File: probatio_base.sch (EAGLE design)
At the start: 12 parts

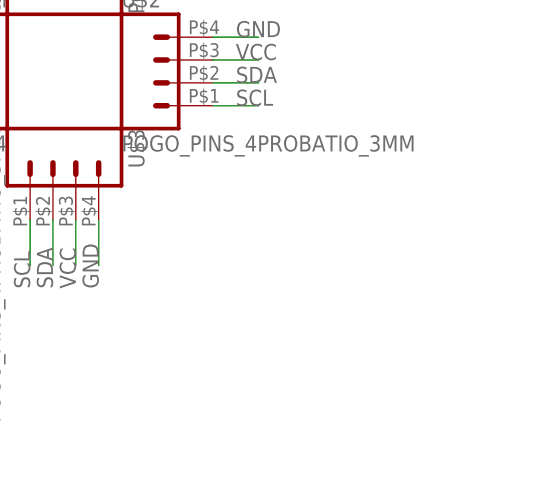
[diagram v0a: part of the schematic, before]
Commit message: added batebit logo
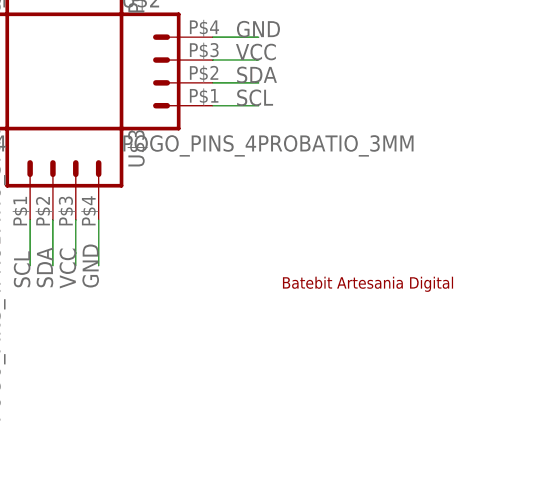
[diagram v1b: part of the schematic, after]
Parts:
- added U$13: BATEBIT_PEQ, Batebit:BATEBIT_PEQ
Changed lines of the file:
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@@
 <part name="U$11" library="Batebit" deviceset="M04" device="WIRE_PAD"/>
 <part name="U$12" library="Batebit" deviceset="M04" device="WIRE_PAD"/>
+<part name="U$13" library="Batebit" deviceset="BATEBIT" device="_PEQ"/>
 </parts>
 <sheets>
@@
 <instance part="U$11" gate="G$1" x="-104.14" y="-17.78"/>
 <instance part="U$12" gate="G$1" x="-78.74" y="-17.78"/>
+<instance part="U$13" gate="G$1" x="38.1" y="-22.86"/>
 </instances>
 <busses>

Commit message: Bug fix: changing layers of pads
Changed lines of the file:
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@@
 <?xml version="1.0" encoding="utf-8"?>
 <!DOCTYPE eagle SYSTEM "eagle.dtd">
-<eagle version="8.2.1">
+<eagle version="9.4.0">
 <drawing>
 <settings>
 <setting alwaysvectorfont="no"/>
+<setting keepoldvectorfont="yes"/>
 <setting verticaltext="up"/>
 </settings>
@@
 </plain>
 <instances>
-<instance part="U$1" gate="G$1" x="2.54" y="12.7" rot="R90"/>
-<instance part="U$2" gate="G$1" x="12.7" y="0"/>
-<instance part="U$3" gate="G$1" x="0" y="-10.16" rot="R270"/>
-<instance part="U$4" gate="G$1" x="-10.16" y="2.54" rot="R180"/>
-<instance part="U$5" gate="G$1" x="-104.14" y="45.72"/>
-<instance part="U$9" gate="G$1" x="-78.74" y="45.72"/>
-<instance part="U$6" gate="G$1" x="-104.14" y="25.4"/>
-<instance part="U$7" gate="G$1" x="-78.74" y="25.4"/>
-<instance part="U$8" gate="G$1" x="-104.14" y="2.54"/>
-<instance part="U$10" gate="G$1" x="-78.74" y="2.54"/>
-<instance part="U$11" gate="G$1" x="-104.14" y="-17.78"/>
-<instance part="U$12" gate="G$1" x="-78.74" y="-17.78"/>
-<instance part="U$13" gate="G$1" x="38.1" y="-22.86"/>
+<instance part="U$1" gate="G$1" x="2.54" y="12.7" smashed="yes" rot="R90">
+<attribute name="VALUE" x="10.16" y="7.62" size="1.778" layer="96" rot="R90"/>
+<attribute name="NAME" x="-5.842" y="7.62" size="1.778" layer="95" rot="R90"/>
+</instance>
+<instance part="U$2" gate="G$1" x="12.7" y="0" smashed="yes">
+<attribute name="VALUE" x="7.62" y="-7.62" size="1.778" layer="96"/>
+<attribute name="NAME" x="7.62" y="8.382" size="1.778" layer="95"/>
+</instance>
+<instance part="U$3" gate="G$1" x="0" y="-10.16" smashed="yes" rot="R270">
+<attribute name="VALUE" x="-7.62" y="-5.08" size="1.778" layer="96" rot="R270"/>
+<attribute name="NAME" x="8.382" y="-5.08" size="1.778" layer="95" rot="R270"/>
+</instance>
+<instance part="U$4" gate="G$1" x="-10.16" y="2.54" smashed="yes" rot="R180">
+<attribute name="VALUE" x="-5.08" y="10.16" size="1.778" layer="96" rot="R180"/>
+<attribute name="NAME" x="-5.08" y="-5.842" size="1.778" layer="95" rot="R180"/>
+</instance>
+<instance part="U$5" gate="G$1" x="-104.14" y="45.72" smashed="yes">
+<attribute name="VALUE" x="-109.22" y="38.1" size="1.778" layer="96"/>
+<attribute name="NAME" x="-109.22" y="54.102" size="1.778" layer="95"/>
+</instance>
+<instance part="U$9" gate="G$1" x="-78.74" y="45.72" smashed="yes">
+<attribute name="VALUE" x="-83.82" y="38.1" size="1.778" layer="96"/>
+<attribute name="NAME" x="-83.82" y="54.102" size="1.778" layer="95"/>
+</instance>
+<instance part="U$6" gate="G$1" x="-104.14" y="25.4" smashed="yes">
+<attribute name="VALUE" x="-109.22" y="17.78" size="1.778" layer="96"/>
+<attribute name="NAME" x="-109.22" y="33.782" size="1.778" layer="95"/>
+</instance>
+<instance part="U$7" gate="G$1" x="-78.74" y="25.4" smashed="yes">
+<attribute name="VALUE" x="-83.82" y="17.78" size="1.778" layer="96"/>
+<attribute name="NAME" x="-83.82" y="33.782" size="1.778" layer="95"/>
+</instance>
+<instance part="U$8" gate="G$1" x="-104.14" y="2.54" smashed="yes">
+<attribute name="VALUE" x="-109.22" y="-5.08" size="1.778" layer="96"/>
+<attribute name="NAME" x="-109.22" y="10.922" size="1.778" layer="95"/>
+</instance>
+<instance part="U$10" gate="G$1" x="-78.74" y="2.54" smashed="yes">
+<attribute name="VALUE" x="-83.82" y="-5.08" size="1.778" layer="96"/>
+<attribute name="NAME" x="-83.82" y="10.922" size="1.778" layer="95"/>
+</instance>
+<instance part="U$11" gate="G$1" x="-104.14" y="-17.78" smashed="yes">
+<attribute name="VALUE" x="-109.22" y="-25.4" size="1.778" layer="96"/>
+<attribute name="NAME" x="-109.22" y="-9.398" size="1.778" layer="95"/>
+</instance>
+<instance part="U$12" gate="G$1" x="-78.74" y="-17.78" smashed="yes">
+<attribute name="VALUE" x="-83.82" y="-25.4" size="1.778" layer="96"/>
+<attribute name="NAME" x="-83.82" y="-9.398" size="1.778" layer="95"/>
+</instance>
+<instance part="U$13" gate="G$1" x="38.1" y="-22.86" smashed="yes"/>
 </instances>
 <busses>
